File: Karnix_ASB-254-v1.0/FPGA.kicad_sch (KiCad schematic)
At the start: 48 parts, among them U5 LFE5U-25F-BG256C, U7 W25Q128JVPIQ, Y2 25 MHz

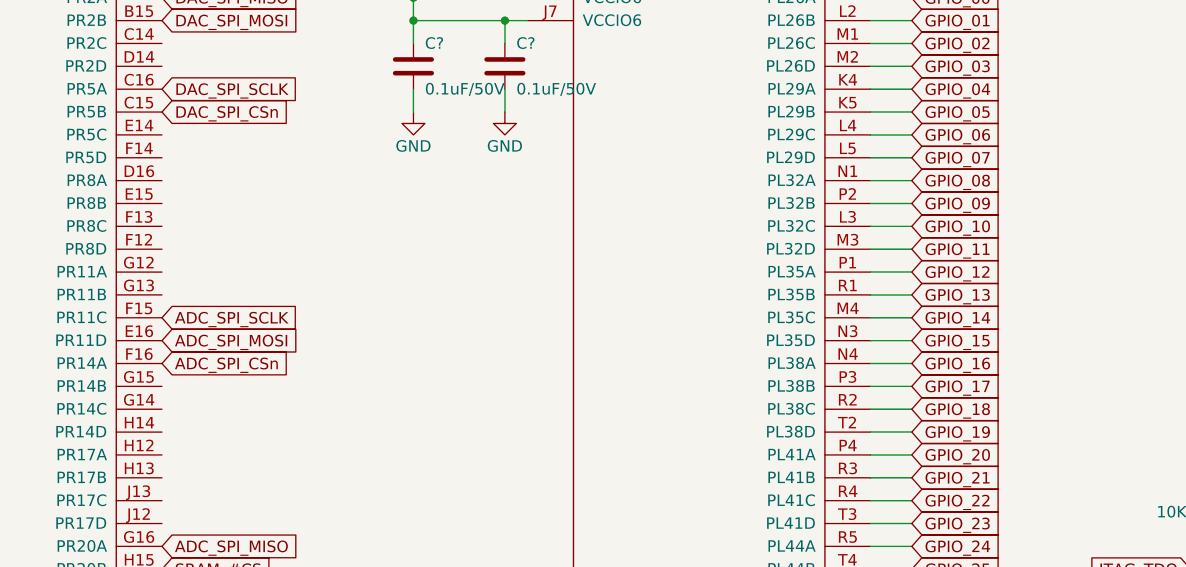
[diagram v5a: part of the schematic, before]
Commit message: Move GPIO_17 to different pin to ease routing
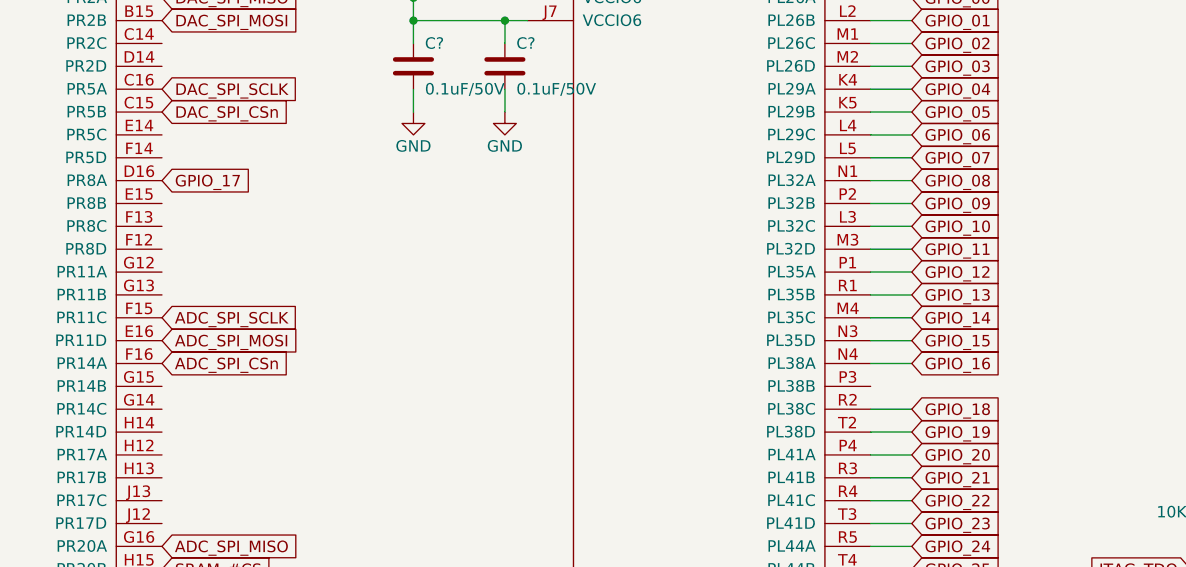
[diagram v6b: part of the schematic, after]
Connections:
- net GPIO_17: now also U5.D16 (PR8A); no longer U5.P3 (PL38B)
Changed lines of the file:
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@@
-    (stroke (width 0) (type default))
-  )
-  (wire (pts (xy 240.157 76.835) (xy 235.585 76.835))
     (stroke (width 0) (type default))
   )
@@
     )
   )
-  (global_label "GPIO_17" (shape input) (at 240.157 76.835 0)
-    (effects (font (size 1.27 1.27)) (justify left))
-    (property "Intersheetrefs" "${INTERSHEET_REFS}" (at 240.157 76.835 0)
-      (effects (font (size 1.27 1.27)) hide)
-    )
+  (global_label "GPIO_17" (shape input) (at 156.845 53.975 0)
+    (effects (font (size 1.27 1.27)) (justify left))
+    (property "Intersheetrefs" "${INTERSHEET_REFS}" (at 156.845 53.975 0)
+      (effects (font (size 1.27 1.27)) hide)
+    )
